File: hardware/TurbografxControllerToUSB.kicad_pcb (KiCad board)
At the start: 2 copper layers, 39.6 x 49.4 mm, 13 parts, among them CON1 AVR-ISP6, J1 USB, J2 DIN8, U1 ATMEGA32U2-AU, X1 16Mhz

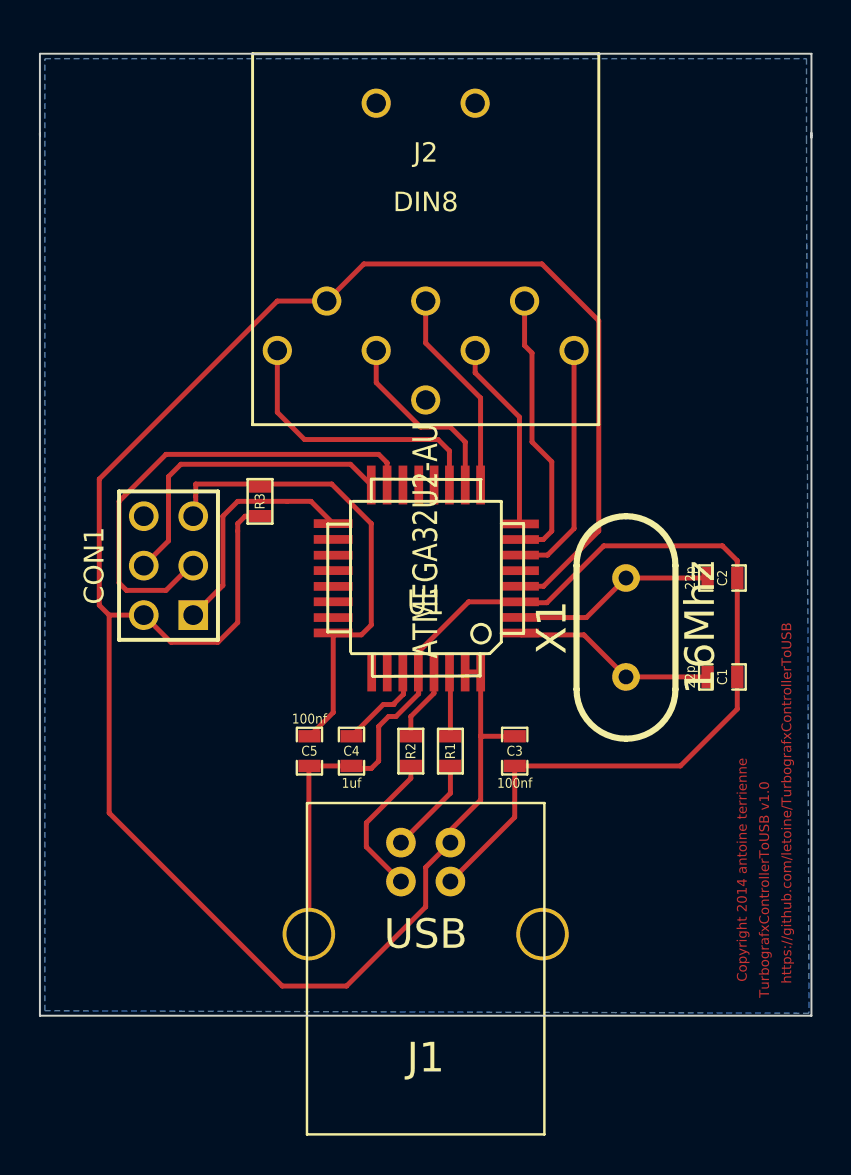
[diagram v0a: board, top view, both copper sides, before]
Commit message: Slim down the board. Add footprind for mini-din8 on top of din8, this will allow to populate with both. Removing some kicad temp files.
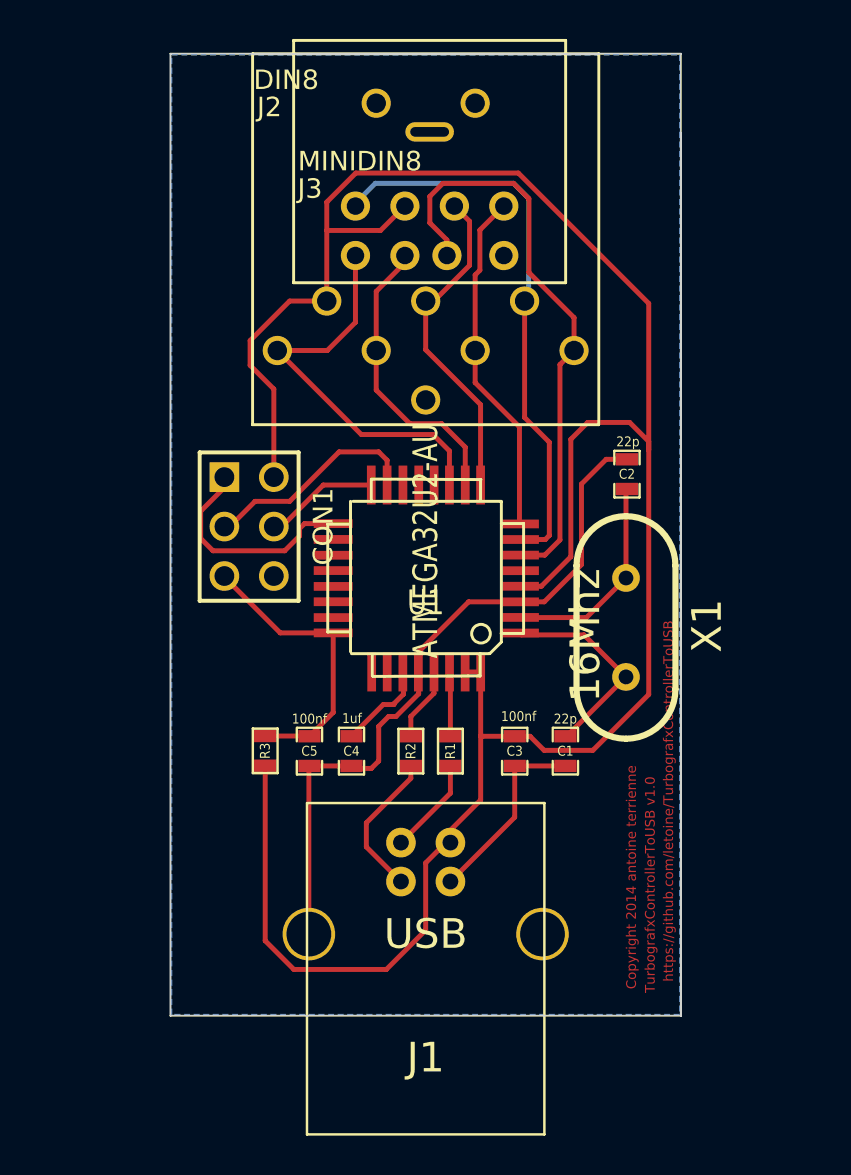
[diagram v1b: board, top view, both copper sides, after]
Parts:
- added J3: MINIDIN8, MINIDIN-8-FEMALE, F.Cu at (210.8, 115.9)
- moved R3 12.8 mm to (202.3, 152.4)
- moved C1 8.92 mm to (217.7, 152.4), turned to 270 degrees
- moved C2 7.24 mm to (220.9, 138.2), turned to 90 degrees
- moved CON1 4.60 mm to (201.5, 140.9), turned to 270 degrees
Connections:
- net DOWN_SELECT_BUTTON renamed DATA2
- net LEFT_RUN_BUTTON renamed DATA3
- net RIGHT_II_BUTTON renamed DATA1
- net UP_I_BUTTON renamed DATA0
- J2 pad 9: (no net) -> GND
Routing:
- net GND: track 65.6 -> 46.2 mm
- net ~OE~: track 12.5 -> 30.3 mm
- net DATA1: track 14.2 -> 29.3 mm
- net SCK: track 24.8 -> 11.4 mm
- net MOSI: track 16.2 -> 5.89 mm
- net RESET: track 24.9 -> 14.9 mm
- net DATA3: track 9.85 -> 17.9 mm
- net DATA0: track 10.6 -> 17.0 mm
- net DATA_SELECT: track 14.6 -> 20.8 mm
- net DATA2: track 9.70 -> 15.2 mm
- net VCC: track 116.4 -> 120.8 mm
- net MISO: track 12.2 -> 11.5 mm
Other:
- board size 39.6 x 49.4 mm -> 26.2 x 49.4 mm
